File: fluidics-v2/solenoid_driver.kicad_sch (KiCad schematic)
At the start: 2 parts, among them J5 Screw_Terminal_01x08, U1 TPL7407LDR

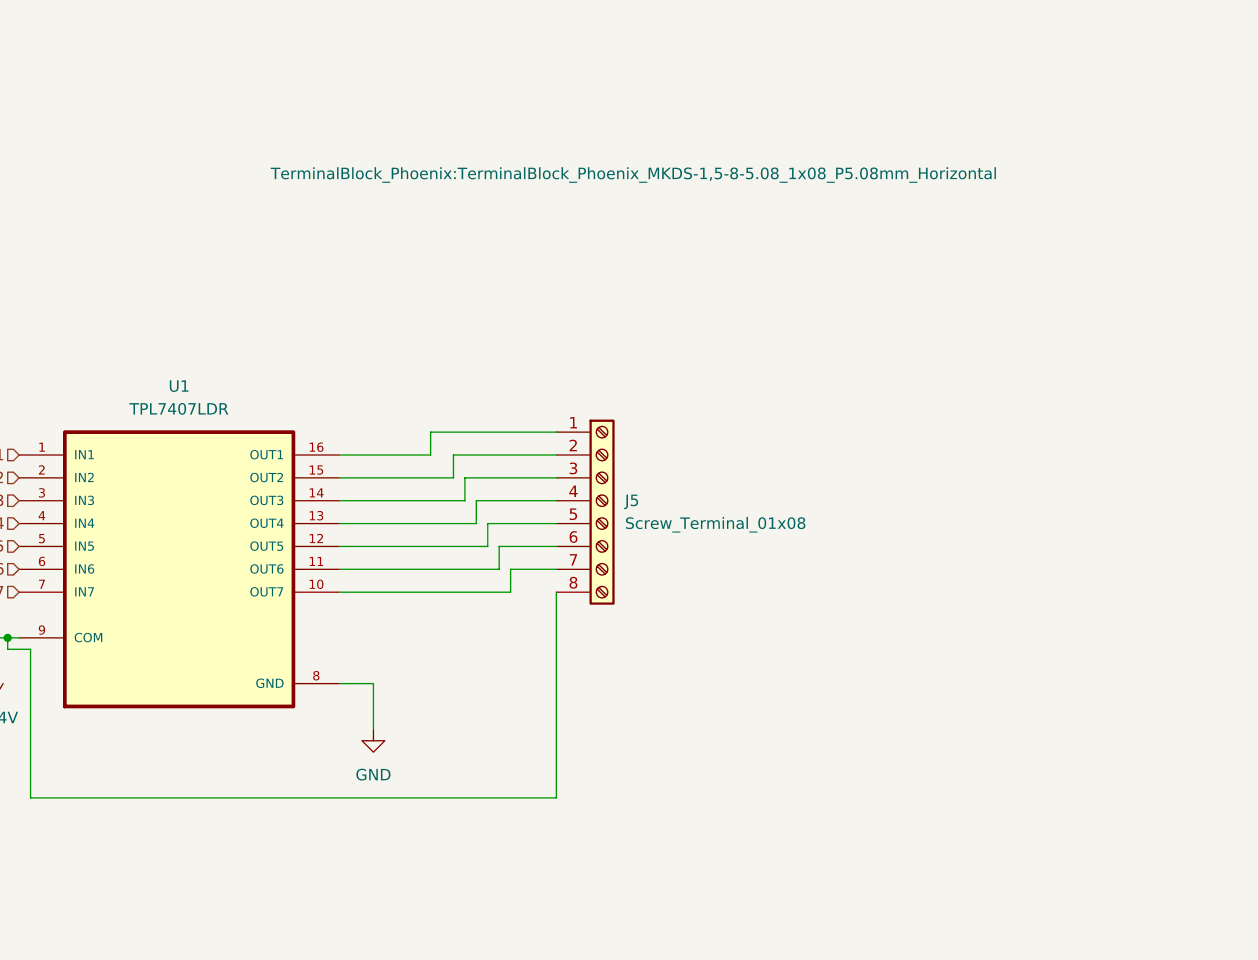
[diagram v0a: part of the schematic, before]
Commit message: Trim board: remove D1/D5-D8/R1/R2/R6-R8/H1, add connector J6
PCB + root schematic + solenoid_driver sheet edits (GUI-driven).
Footprints 85 -> 75. Removed diodes D1/D5-D8, resistors R1/R2/R6-R8,
mounting hole H1; added connector J6. Schematic/PCB in parity
(kicad-cli drc: schematic_parity 0). Remaining DRC items are the
inherited-from-upstream cosmetic set (silk_over_copper, malformed
_courtyard, lib_footprint_mismatch) plus 5 intentional no-connects
and 1 dangling track.

Co-Authored-By: Claude Opus 4.8 (1M context) <noreply@anthropic.com>
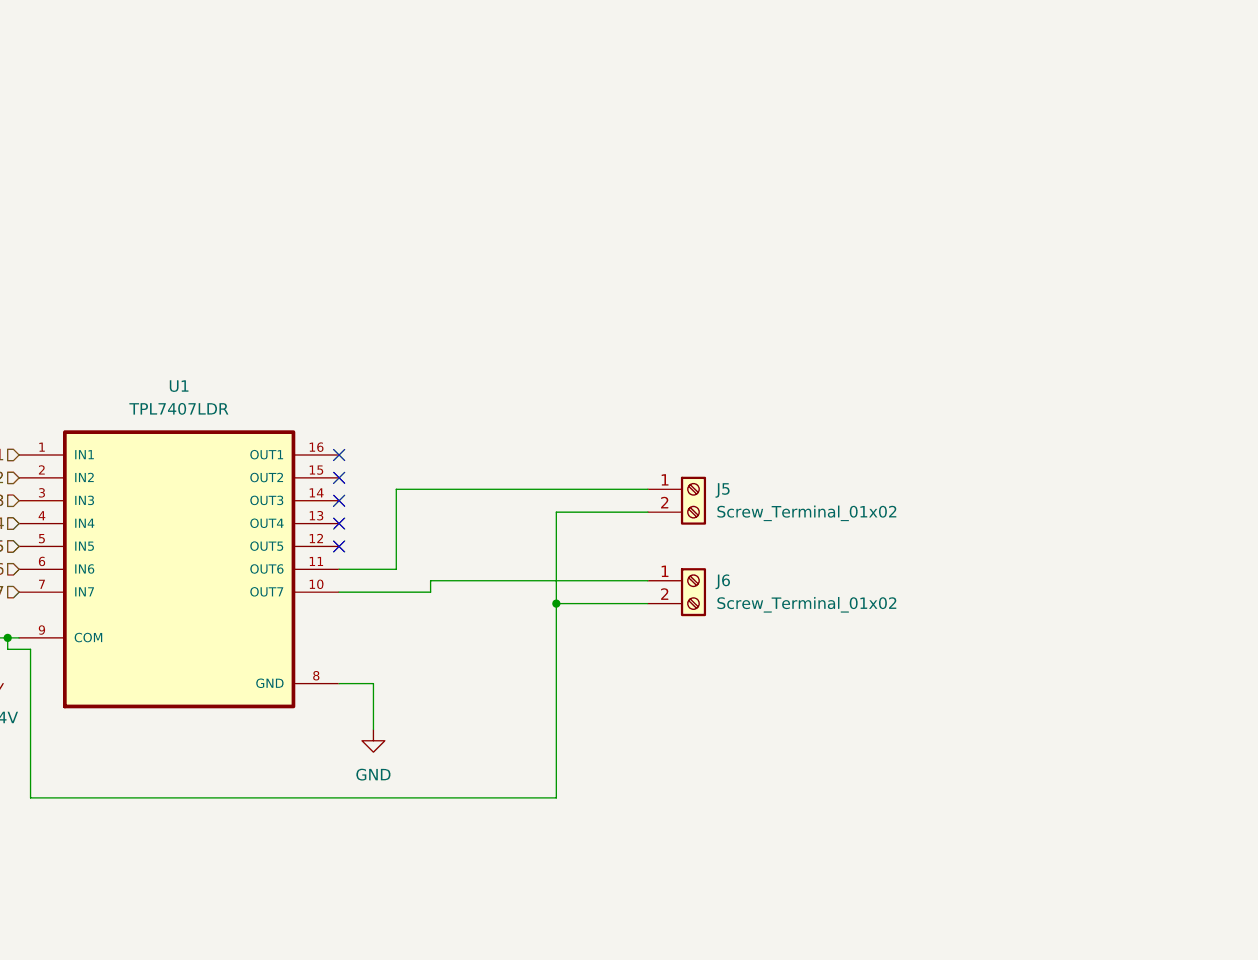
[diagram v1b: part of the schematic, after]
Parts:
- removed J5: Screw_Terminal_01x08, TerminalBlock_Phoenix:TerminalBlock_Phoenix_MKDS-1,5-8-5.08_1x08_P5.08mm_Horizontal, symbol Connector:Screw_Terminal_01x08
- added J5, J6: Screw_Terminal_01x02, TerminalBlock_Phoenix:TerminalBlock_Phoenix_MKDS-1,5-2-5.08_1x02_P5.08mm_Horizontal, symbol Connector:Screw_Terminal_01x02
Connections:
- net +24V: now also J5.2 (Pin_2), J6.2 (Pin_2)
- net at U1.10 (OUT7): now also J6.1 (Pin_1)
- net at U1.11 (OUT6): now also J5.1 (Pin_1)
- no-connect marks 0 -> 5
